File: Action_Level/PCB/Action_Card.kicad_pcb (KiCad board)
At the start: 2 copper layers, 100 x 60 mm, 81 parts, among them J1 Conn_01x03, J2 Conn_01x03, J3 Conn_01x04, SW1 SW_DPDT_x2, U1 txb0108, U10 Trou-3, U11 Trou-3, U12 Trou-3, U13 Trou-3, U2 txb0108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

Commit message: End of the route step
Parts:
- moved C4 8.23 mm to (144.9, 89.4), turned to 90 degrees
- moved C2 3.99 mm to (145.5, 95.9), turned to 90 degrees
- moved C1 1.97 mm to (147.9, 95.9), turned to 270 degrees
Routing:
- net GND: track 298.0 -> 527.6 mm, vias 0 -> 14
- net +3V3: track 102.2 -> 270.8 mm, vias 0 -> 7
- net Net-(J_SENSOR_AR1-Pad2): track 0.00 -> 168.2 mm, vias 0 -> 5
- net /Communication-Part/SDA(5V): track 3.40 -> 138.7 mm, vias 0 -> 2
- net /Communication-Part/SCL(5V): track 3.46 -> 124.2 mm, vias 0 -> 4
- net Net-(J_SENSOR_AV1-Pad2): track 0.00 -> 110.2 mm, vias 0 -> 4
- net +5V: track 210.7 -> 318.9 mm, vias 2 -> 9
- net /Controller-Part/DIR_PaP: track 0.00 -> 88.1 mm, vias 0 -> 4
- net /Controller-Part/STEP_PaP: track 0.00 -> 75.0 mm, vias 0 -> 4
- net +12VA: track 155.8 -> 222.7 mm, vias 0 -> 2
- net /Communication-Part/nrst(3V3): track 2.66 -> 64.5 mm, vias 0 -> 3
- net GNDPWR: track 213.2 -> 272.4 mm, vias 0 -> 2
- net /Controller-Part/~EN~_PaP-R: track 3.32 -> 60.8 mm, vias 0 -> 4
- net Net-(J_FC_RB1-Pad2): track 0.00 -> 54.7 mm
- net Net-(J_FC_RT1-Pad2): track 0.00 -> 51.3 mm
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
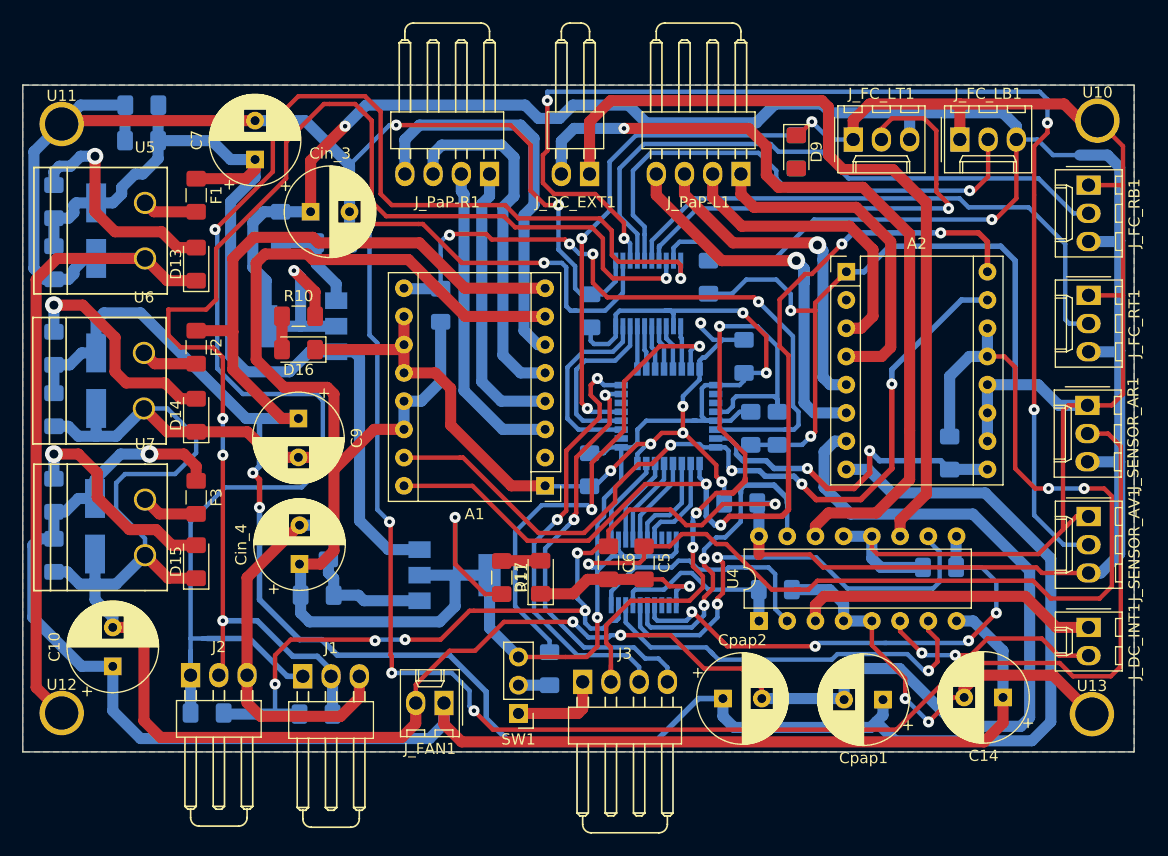
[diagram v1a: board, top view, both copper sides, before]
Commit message: Debug of route part + 3dshapes
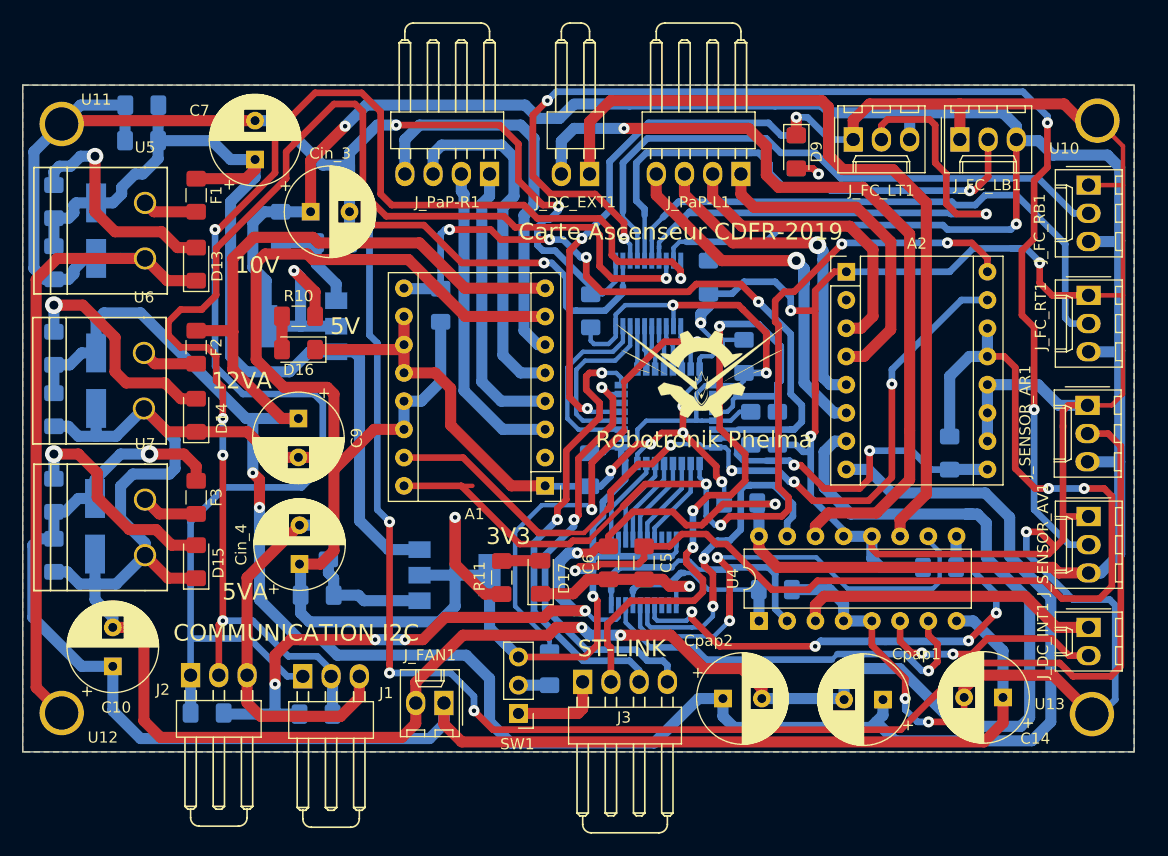
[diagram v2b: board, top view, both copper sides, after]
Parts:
- added G***: LOGO, Logo:LOGO, F.Cu at (141.0, 90.3)
- U5, U6, U7: footprint B plug:B plug 5mm -> B plug:Bplug-5mm
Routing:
- net GND: track 527.6 -> 617.4 mm, vias 14 -> 16
- net /Controller-Part/EN_DC_EXT: track 45.3 -> 66.7 mm
- net +5V: track 318.9 -> 339.2 mm
- net /Communication-Part/SDA(5V): track 138.7 -> 157.4 mm
- net Net-(J_SENSOR_AR1-Pad2): track 168.2 -> 185.5 mm
- net /Controller-Part/~EN~_PaP-R: track 60.8 -> 77.8 mm
- net /Communication-Part/nrst(3V3): track 64.5 -> 76.0 mm
- net /Controller-Part/PWM_R-DC_INT: track 36.4 -> 46.4 mm
- net /Controller-Part/PWM_L-DC_INT: track 23.0 -> 32.7 mm
- net Net-(J_DC_INT1-Pad2): track 20.0 -> 28.5 mm
- net Net-(J_FC_LT1-Pad2): track 43.2 -> 50.6 mm
- net +3V3: track 270.8 -> 278.2 mm
- net /Controller-Part/PWM_L-DC_EXT: track 41.6 -> 48.3 mm
- net /Controller-Part/PWM_R-DC_EXT: track 29.8 -> 35.5 mm
- net /Controller-Part/DIR_PaP: track 88.1 -> 93.4 mm
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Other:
- net class Default: trace_width 0.4 -> 0.6
- board text added: "10V"
- board text added: "12VA"
- board text added: "3V3"
- board text added: "5V"
- board text added: "5VA"
- board text added: "COMMUNICATION I2C"
- board text added: "Carte Ascenseur CDFR-2019"
- board text added: "Robotronik Phelma"
- board text added: "ST-LINK"
